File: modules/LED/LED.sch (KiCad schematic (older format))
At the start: 48 parts, among them J1 2, J10 11, J11 12, J12 13, J13 A0, J14 A1, J15 A2, J16 A3, J17 A4, J18 A5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

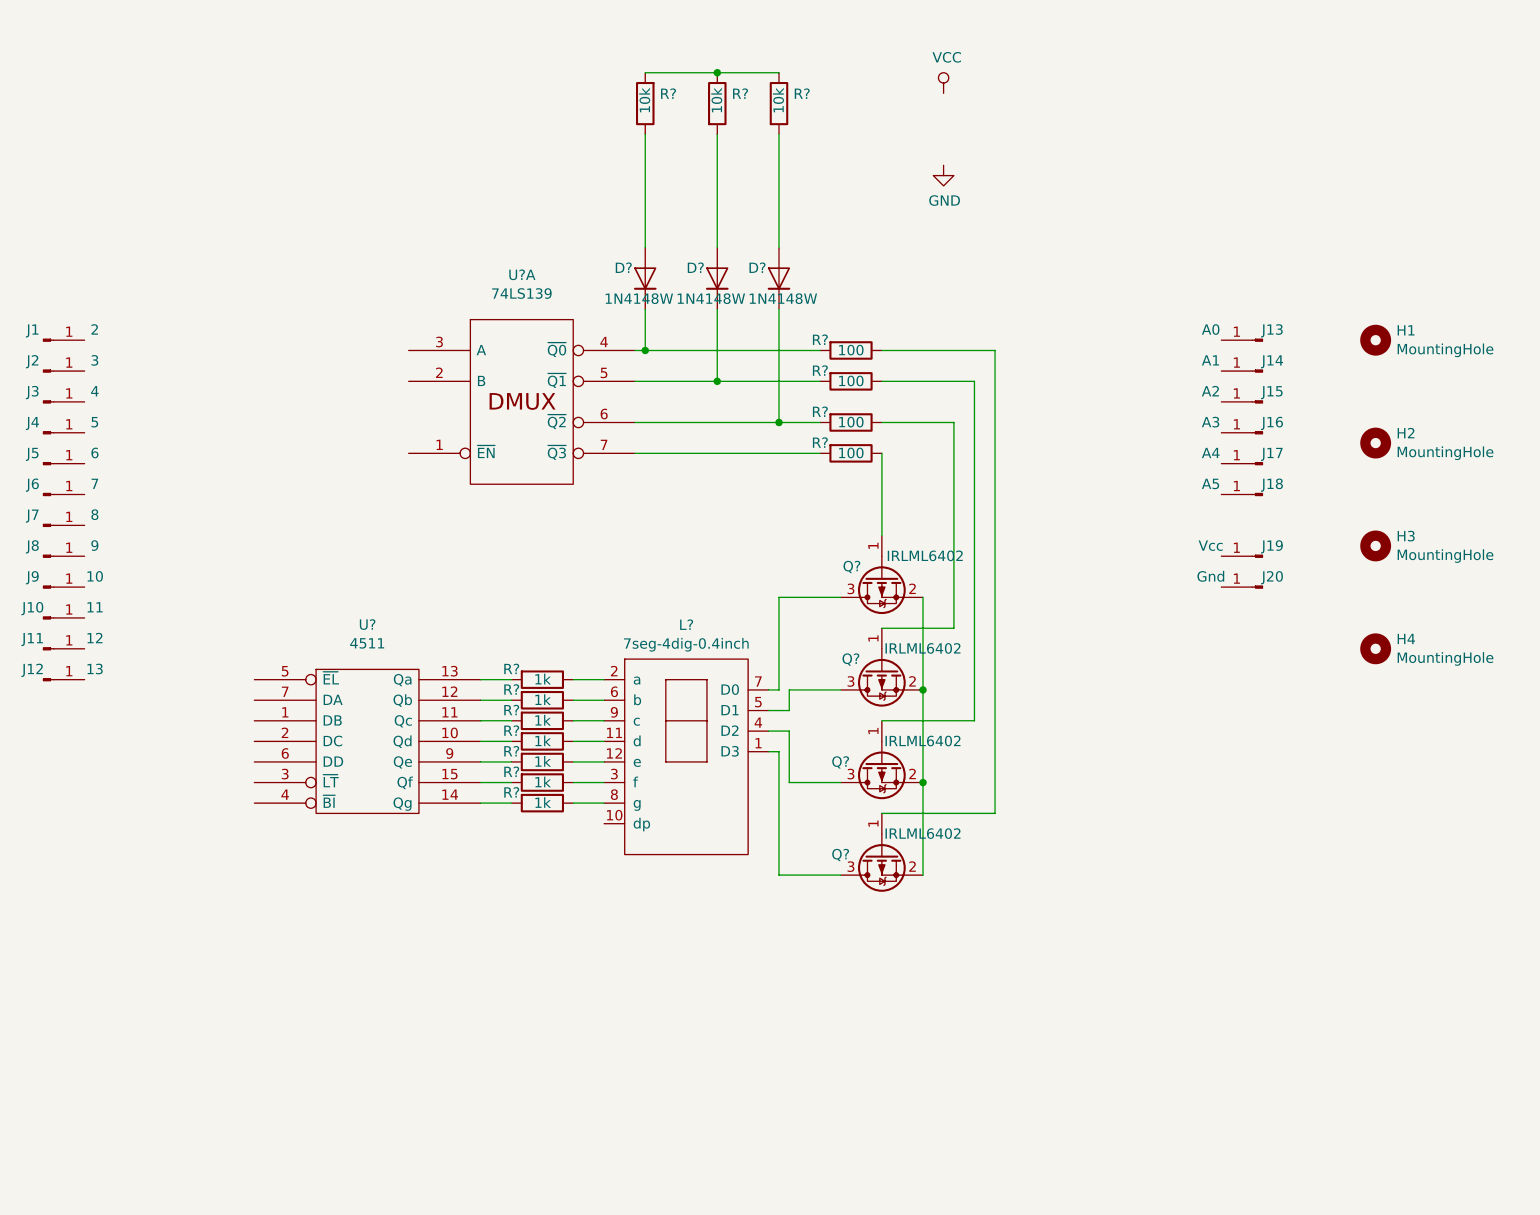
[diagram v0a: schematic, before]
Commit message: Add buttons. Place components on PCB.
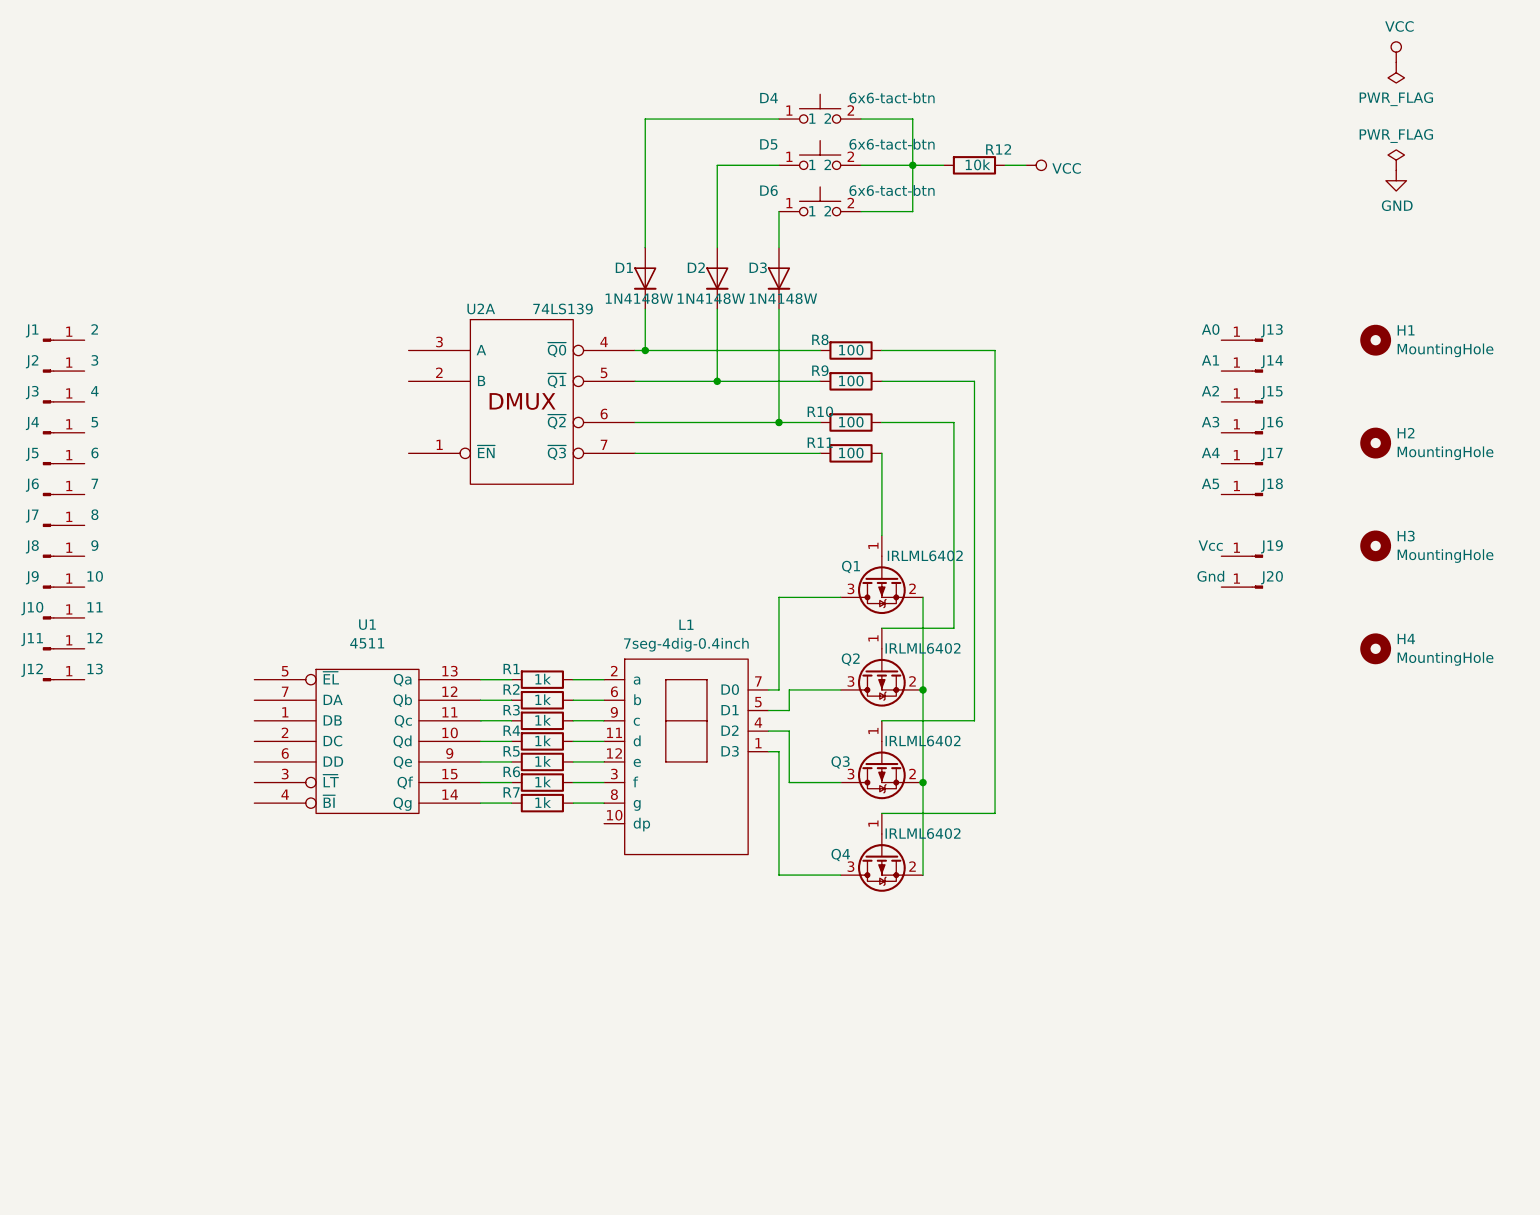
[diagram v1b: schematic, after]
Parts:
- removed R? (x2): 10k, symbol Device:R
- added D4, D5, D6: 6x6-tact-btn, CommonLibrary:6x6-tact-btn, symbol CommonLibrary:6x6-tact-btn
- L1: renamed from L?; footprint (none) -> CommonLibrary:7seg-4dig-0.4inch
- R1, R10, R11, R12, R2, R3, R4, R5, R6, R7, R8, R9: renamed from R?; footprint (none) -> Resistor_SMD:R_0805_2012Metric_Pad1.15x1.40mm_HandSolder
- U1, U2: renamed from U?; footprint (none) -> Package_SO:SOIC-16_3.9x9.9mm_P1.27mm
- gave numbers to parts that had none: 7
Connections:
- net VCC: now also R12.1
- net at D3.2 (A): now also D6.1
- net at D2.2 (A): now also D5.1; no longer R12.2
- net at D1.2 (A): now also D4.1
- new net: D4.2, D5.2, D6.2, R12.2
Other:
- moved on the sheet: R12

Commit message: In work
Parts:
- added R13: 10k, Resistor_SMD:R_0805_2012Metric_Pad1.15x1.40mm_HandSolder, symbol Device:R
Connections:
- wire segments 61 -> 94
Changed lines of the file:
@@
 U 1 1 5D7A9916
 P 2600 4450
-F 0 "U1" H 2600 5016 50  0000 C CNN
-F 1 "4511" H 2600 4925 50  0000 C CNN
+F 0 "U1" H 2400 4850 50  0000 C CNN
+F 1 "4511" H 2800 4850 50  0000 C CNN
 F 2 "Package_SO:SOIC-16_3.9x9.9mm_P1.27mm" H 2600 4450 50  0001 C CNN
 F 3 "" H 2600 4450 50  0001 C CNN
@@
 Wire Wire Line
 	5700 1650 5800 1650
+Connection ~ 5250 1650
+Wire Wire Line
+	5250 1650 5400 1650
+Wire Wire Line
+	5250 1875 5250 1650
+$Comp
+L power:GND #PWR02
+U 1 1 5D7C0B09
+P 2600 4900
+F 0 "#PWR02" H 2600 4650 50  0001 C CNN
+F 1 "GND" H 2605 4727 50  0000 C CNN
+F 2 "" H 2600 4900 50  0001 C CNN
+F 3 "" H 2600 4900 50  0001 C CNN
+	1    2600 4900
+	1    0    0    -1
+$EndComp
+Wire Wire Line
+	2600 4900 2600 4800
+$Comp
+L power:VCC #PWR01
+U 1 1 5D7C2BA3
+P 2600 4000
+F 0 "#PWR01" H 2600 3850 50  0001 C CNN
+F 1 "VCC" H 2617 4173 50  0000 C CNN
+F 2 "" H 2600 4000 50  0001 C CNN
+F 3 "" H 2600 4000 50  0001 C CNN
+	1    2600 4000
+	1    0    0    -1
+$EndComp
+Wire Wire Line
+	2600 4000 2600 4100
+$Comp
+L power:VCC #PWR03
+U 1 1 5D7C9673
+P 6500 3550
+F 0 "#PWR03" H 6500 3400 50  0001 C CNN
+F 1 "VCC" H 6517 3723 50  0000 C CNN
+F 2 "" H 6500 3550 50  0001 C CNN
+F 3 "" H 6500 3550 50  0001 C CNN
+	1    6500 3550
+	1    0    0    -1
+$EndComp
+$Comp
+L power:GND #PWR04
+U 1 1 5D7CA139
+P 6500 3700
+F 0 "#PWR04" H 6500 3450 50  0001 C CNN
+F 1 "GND" H 6505 3527 50  0000 C CNN
+F 2 "" H 6500 3700 50  0001 C CNN
+F 3 "" H 6500 3700 50  0001 C CNN
+	1    6500 3700
+	1    0    0    -1
+$EndComp
+Wire Wire Line
+	6500 3550 6750 3550
+Wire Wire Line
+	6500 3700 6750 3700
+Wire Wire Line
+	2000 2500 2000 1000
+Wire Wire Line
+	2000 1000 5250 1000
+Wire Wire Line
+	5250 1000 5250 1425
+Connection ~ 5250 1425
 Wire Wire Line
 	5250 1425 5250 1650
-Connection ~ 5250 1650
-Wire Wire Line
-	5250 1650 5400 1650
-Wire Wire Line
-	5250 1875 5250 1650
+Wire Wire Line
+	1200 2500 1225 2500
+Connection ~ 1225 2500
+Wire Wire Line
+	1225 2500 2000 2500
+Wire Wire Line
+	1750 4350 2050 4350
+Wire Wire Line
+	2050 4450 1800 4450
+Wire Wire Line
+	1800 4450 1800 3850
+Wire Wire Line
+	1200 3550 1225 3550
+Wire Wire Line
+	1850 3550 1850 4650
+Wire Wire Line
+	1850 4650 2050 4650
+Connection ~ 1225 3550
+Wire Wire Line
+	1225 3550 1850 3550
+Wire Wire Line
+	1200 3400 1225 3400
+Wire Wire Line
+	1900 3400 1900 4550
+Wire Wire Line
+	1900 4550 2050 4550
+Connection ~ 1225 3400
+Wire Wire Line
+	1225 3400 1900 3400
+Wire Wire Line
+	1200 3250 1225 3250
+Wire Wire Line
+	1700 4000 1700 4250
+Wire Wire Line
+	1200 4000 1225 4000
+Wire Wire Line
+	1700 4250 2050 4250
+Connection ~ 1225 4000
+Wire Wire Line
+	1225 4000 1700 4000
+Wire Wire Line
+	1200 3850 1225 3850
+Connection ~ 1225 3850
+Wire Wire Line
+	1225 3850 1800 3850
+Wire Wire Line
+	1750 3700 1750 4350
+Wire Wire Line
+	1200 3700 1225 3700
+Connection ~ 1225 3700
+Wire Wire Line
+	1225 3700 1750 3700
+$Comp
+L Device:R R13
+U 1 1 5D82C9F4
+P 2050 3800
+F 0 "R13" H 2120 3846 50  0000 L CNN
+F 1 "10k" H 2120 3755 50  0000 L CNN
+F 2 "Resistor_SMD:R_0805_2012Metric_Pad1.15x1.40mm_HandSolder" V 1980 3800 50  0001 C CNN
+F 3 "~" H 2050 3800 50  0001 C CNN
+	1    2050 3800
+	1    0    0    -1
+$EndComp
+Wire Wire Line
+	2050 3950 2050 4150
+Connection ~ 2050 4150
+Wire Wire Line
+	2050 4150 2050 4750
+$Comp
+L power:VCC #PWR0104
+U 1 1 5D837204
+P 2050 3600
+F 0 "#PWR0104" H 2050 3450 50  0001 C CNN
+F 1 "VCC" H 2067 3773 50  0000 C CNN
+F 2 "" H 2050 3600 50  0001 C CNN
+F 3 "" H 2050 3600 50  0001 C CNN
+	1    2050 3600
+	1    0    0    -1
+$EndComp
+Wire Wire Line
+	2050 3600 2050 3650
 $EndSCHEMATC

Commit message: Ready!
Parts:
- removed D3: 1N4148W, Diode_SMD:D_SOD-123, symbol Diode:1N4148W
- removed D6: 6x6-tact-btn, CommonLibrary:6x6-tact-btn, symbol CommonLibrary:6x6-tact-btn
- added C1: 0.1uF, Capacitor_SMD:C_0805_2012Metric_Pad1.15x1.40mm_HandSolder, symbol Device:C
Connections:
- wire segments 94 -> 108
- no-connect marks 0 -> 10
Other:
- moved on the sheet: R13

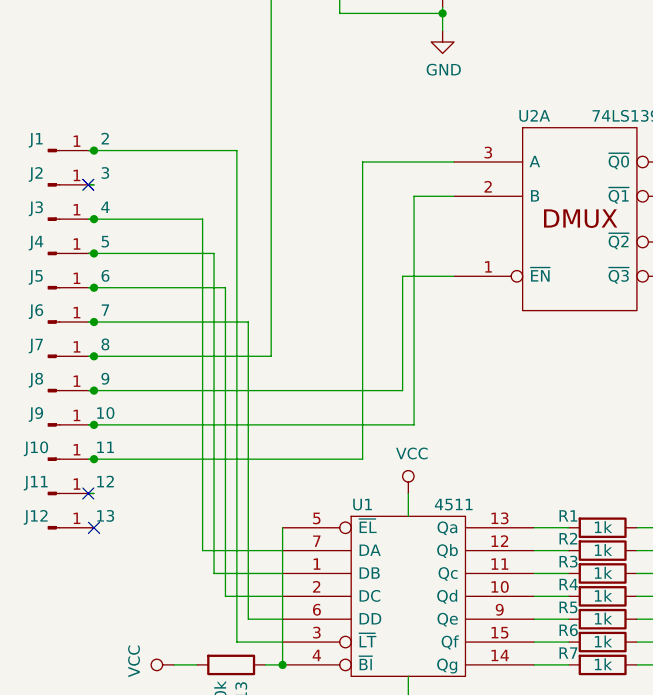
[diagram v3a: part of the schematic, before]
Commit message: A0 == pin 12 A1 == pin 13
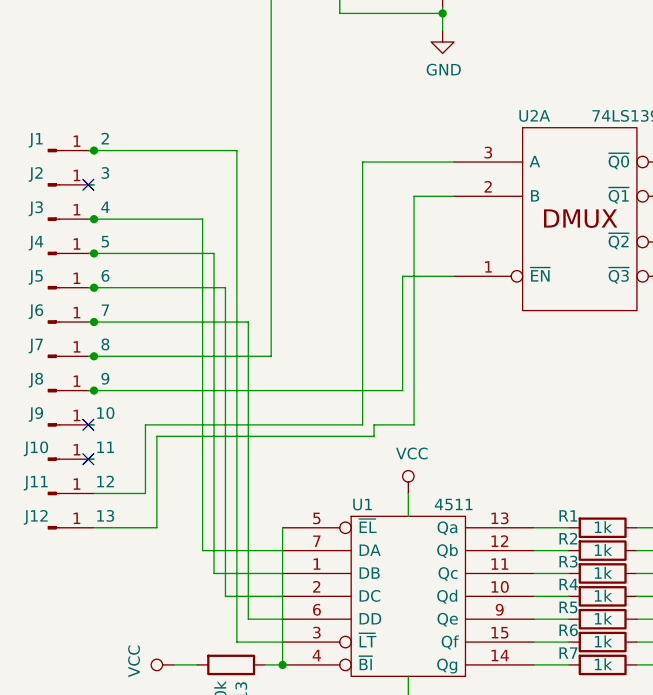
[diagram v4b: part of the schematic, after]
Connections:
- wire segments 108 -> 113
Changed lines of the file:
@@
 	1900 4550 2050 4550
-Wire Wire Line
-	1200 4000 1225 4000
 Wire Wire Line
 	1700 4250 2050 4250
@@
 Wire Wire Line
 	1200 3700 1225 3700
-Connection ~ 1225 3700
-Wire Wire Line
-	1225 3700 2625 3700
-Wire Wire Line
-	2400 3850 2400 2550
 Wire Wire Line
 	1200 3850 1225 3850
 Wire Wire Line
 	2400 2550 2800 2550
-Connection ~ 1225 3850
-Wire Wire Line
-	1225 3850 2400 3850
-NoConn ~ 1200 4000
 NoConn ~ 6750 3250
 NoConn ~ 6750 2500
@@
 NoConn ~ 6750 2950
 NoConn ~ 6750 3100
-NoConn ~ 1225 4150
 NoConn ~ 3750 4850
 $Comp
@@
 	1    0    0    -1
 $EndComp
+Wire Wire Line
+	1450 3700 2400 3700
+Wire Wire Line
+	1450 3700 1450 4000
+Wire Wire Line
+	2400 3700 2400 2550
+Wire Wire Line
+	1500 4150 1500 3750
+Wire Wire Line
+	1500 3750 2450 3750
+Wire Wire Line
+	2450 3750 2450 3700
+Wire Wire Line
+	2450 3700 2625 3700
+Wire Wire Line
+	1225 4150 1500 4150
+Wire Wire Line
+	1225 4000 1450 4000
+NoConn ~ 1200 3700
+NoConn ~ 1200 3850
 $EndSCHEMATC

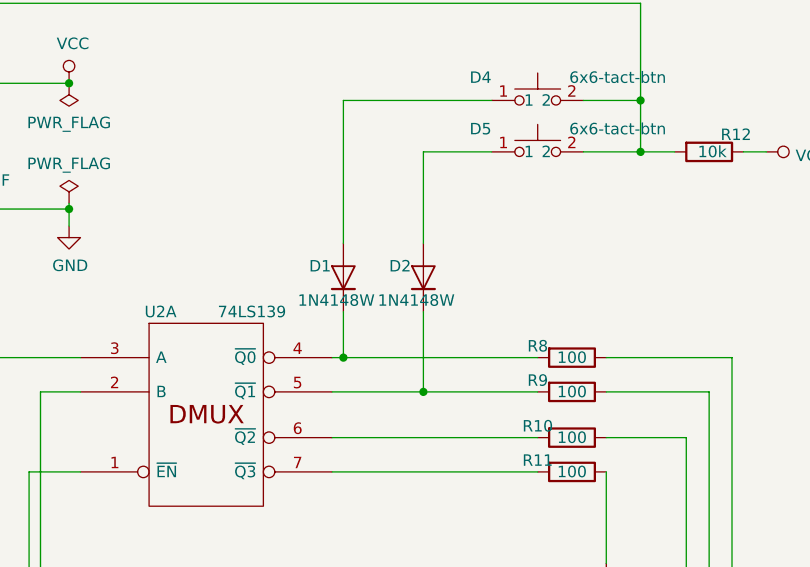
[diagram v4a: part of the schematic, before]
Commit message: Replace 1N4148W -> LL4148
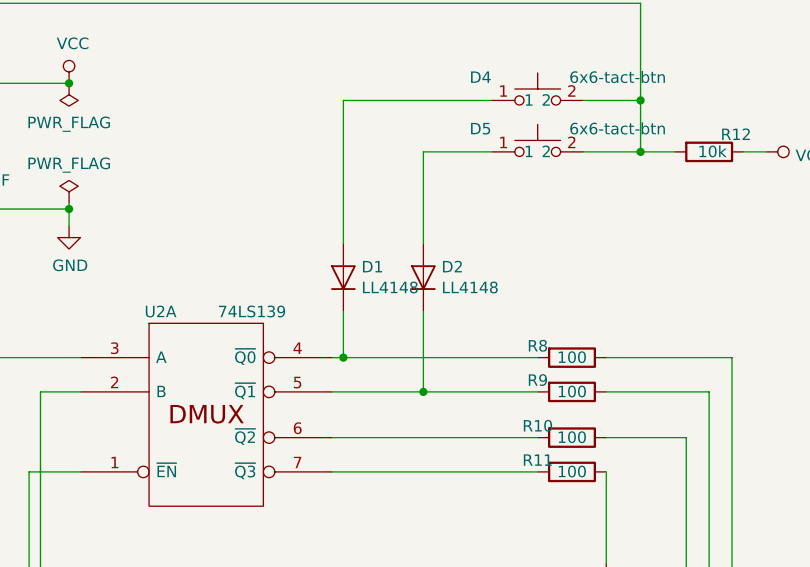
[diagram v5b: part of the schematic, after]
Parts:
- removed D1, D2: 1N4148W, Diode_SMD:D_SOD-123, symbol Diode:1N4148W
- added D1, D2: LL4148, Diode_SMD:D_MiniMELF, symbol Diode:LL4148
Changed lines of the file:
@@
-$EndComp
-$Comp
-L Diode:1N4148W D2
-U 1 1 5D7B1F06
-P 4300 2200
-F 0 "D2" V 4350 2350 50  0000 R CNN
-F 1 "1N4148W" V 4200 2400 50  0000 R CNN
-F 2 "Diode_SMD:D_SOD-123" H 4300 2025 50  0001 C CNN
-F 3 "https://www.vishay.com/docs/85748/1n4148w.pdf" H 4300 2200 50  0001 C CNN
-	1    4300 2200
-	0    -1   -1   0
-$EndComp
-$Comp
-L Diode:1N4148W D1
-U 1 1 5D7B2356
-P 3950 2200
-F 0 "D1" V 4000 2350 50  0000 R CNN
-F 1 "1N4148W" V 3850 2400 50  0000 R CNN
-F 2 "Diode_SMD:D_SOD-123" H 3950 2025 50  0001 C CNN
-F 3 "https://www.vishay.com/docs/85748/1n4148w.pdf" H 3950 2200 50  0001 C CNN
-	1    3950 2200
-	0    -1   -1   0
 $EndComp
 $Comp
@@
 NoConn ~ 1200 3700
 NoConn ~ 1200 3850
+$Comp
+L Diode:LL4148 D1
+U 1 1 5D8A50AE
+P 3950 2200
+F 0 "D1" V 3996 2121 50  0000 R CNN
+F 1 "LL4148" V 3905 2121 50  0000 R CNN
+F 2 "Diode_SMD:D_MiniMELF" H 3950 2025 50  0001 C CNN
+F 3 "http://www.vishay.com/docs/85557/ll4148.pdf" H 3950 2200 50  0001 C CNN
+	1    3950 2200
+	0    -1   -1   0
+$EndComp
+$Comp
+L Diode:LL4148 D2
+U 1 1 5D8A597F
+P 4300 2200
+F 0 "D2" V 4346 2121 50  0000 R CNN
+F 1 "LL4148" V 4255 2121 50  0000 R CNN
+F 2 "Diode_SMD:D_MiniMELF" H 4300 2025 50  0001 C CNN
+F 3 "http://www.vishay.com/docs/85557/ll4148.pdf" H 4300 2200 50  0001 C CNN
+	1    4300 2200
+	0    -1   -1   0
+$EndComp
 $EndSCHEMATC

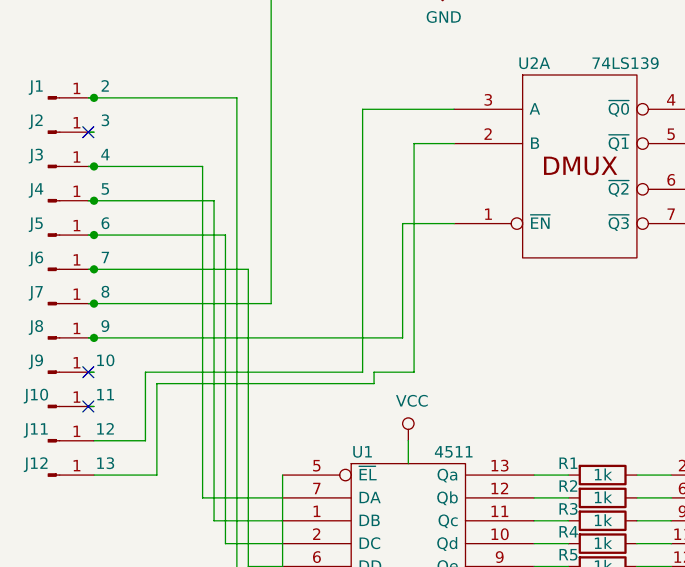
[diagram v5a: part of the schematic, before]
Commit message: Enable pin not required
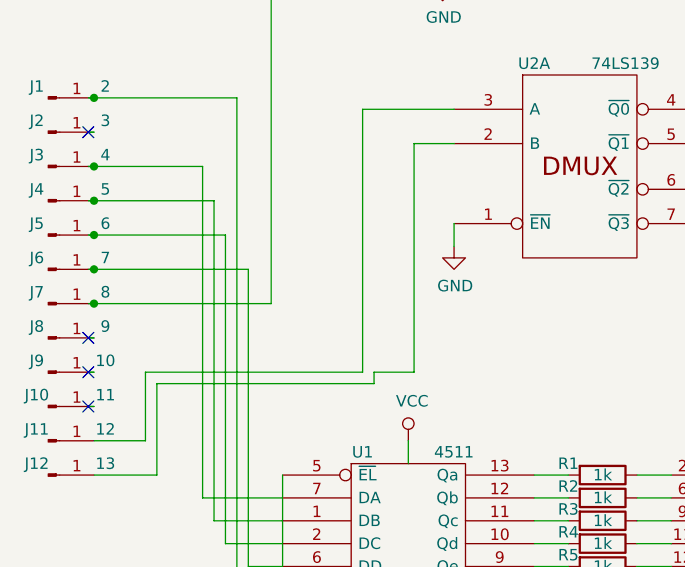
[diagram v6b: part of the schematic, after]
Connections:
- wire segments 113 -> 111
- no-connect marks 10 -> 11
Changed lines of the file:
@@
 Connection ~ 2050 4750
 Wire Wire Line
-	2575 3550 2575 3050
-Wire Wire Line
-	2575 3050 2800 3050
-Wire Wire Line
 	1200 3550 1225 3550
-Connection ~ 1225 3550
-Wire Wire Line
-	1225 3550 2575 3550
 Wire Wire Line
 	2625 3700 2625 2700
@@
 	0    -1   -1   0
 $EndComp
+NoConn ~ 1200 3550
+$Comp
+L power:GND #PWR?
+U 1 1 5D8A7568
+P 2800 3150
+F 0 "#PWR?" H 2800 2900 50  0001 C CNN
+F 1 "GND" H 2805 2977 50  0000 C CNN
+F 2 "" H 2800 3150 50  0001 C CNN
+F 3 "" H 2800 3150 50  0001 C CNN
+	1    2800 3150
+	1    0    0    -1
+$EndComp
+Wire Wire Line
+	2800 3050 2800 3150
 $EndSCHEMATC

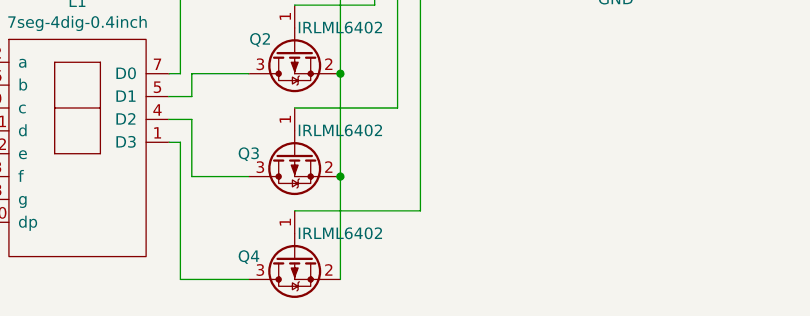
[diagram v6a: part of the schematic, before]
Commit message: Lost Vcc!!!
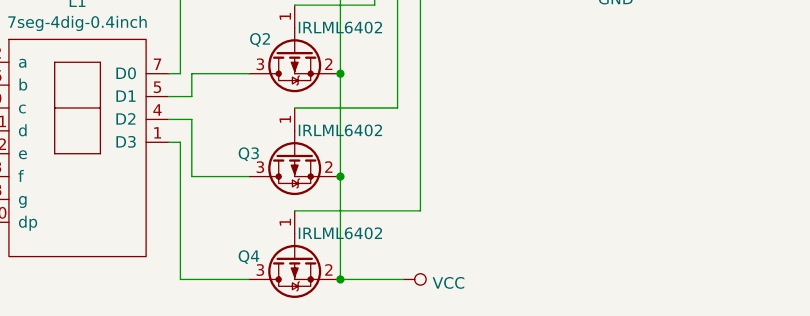
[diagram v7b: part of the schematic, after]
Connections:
- wire segments 111 -> 112
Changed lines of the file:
@@
 Wire Wire Line
 	2800 3050 2800 3150
+$Comp
+L power:VCC #PWR?
+U 1 1 5D9A7B3F
+P 5575 5100
+F 0 "#PWR?" H 5575 4950 50  0001 C CNN
+F 1 "VCC" V 5592 5228 50  0000 L CNN
+F 2 "" H 5575 5100 50  0001 C CNN
+F 3 "" H 5575 5100 50  0001 C CNN
+	1    5575 5100
+	0    1    1    0
+$EndComp
+Wire Wire Line
+	5300 5100 5575 5100
+Connection ~ 5300 5100
 $EndSCHEMATC
